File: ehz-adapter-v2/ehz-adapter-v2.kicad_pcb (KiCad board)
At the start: 2 copper layers, 32 x 32 mm, 16 parts, among them J1 Conn_02x10_Counter_Clockwise, J2 Conn_02x10_Counter_Clockwise, J3 Conn_01x02_Male, Q1 SFH 309 FA-5/6, Q2 BSS138, U1 LMV7235M7X, U2 D-SUN-MP1584EN

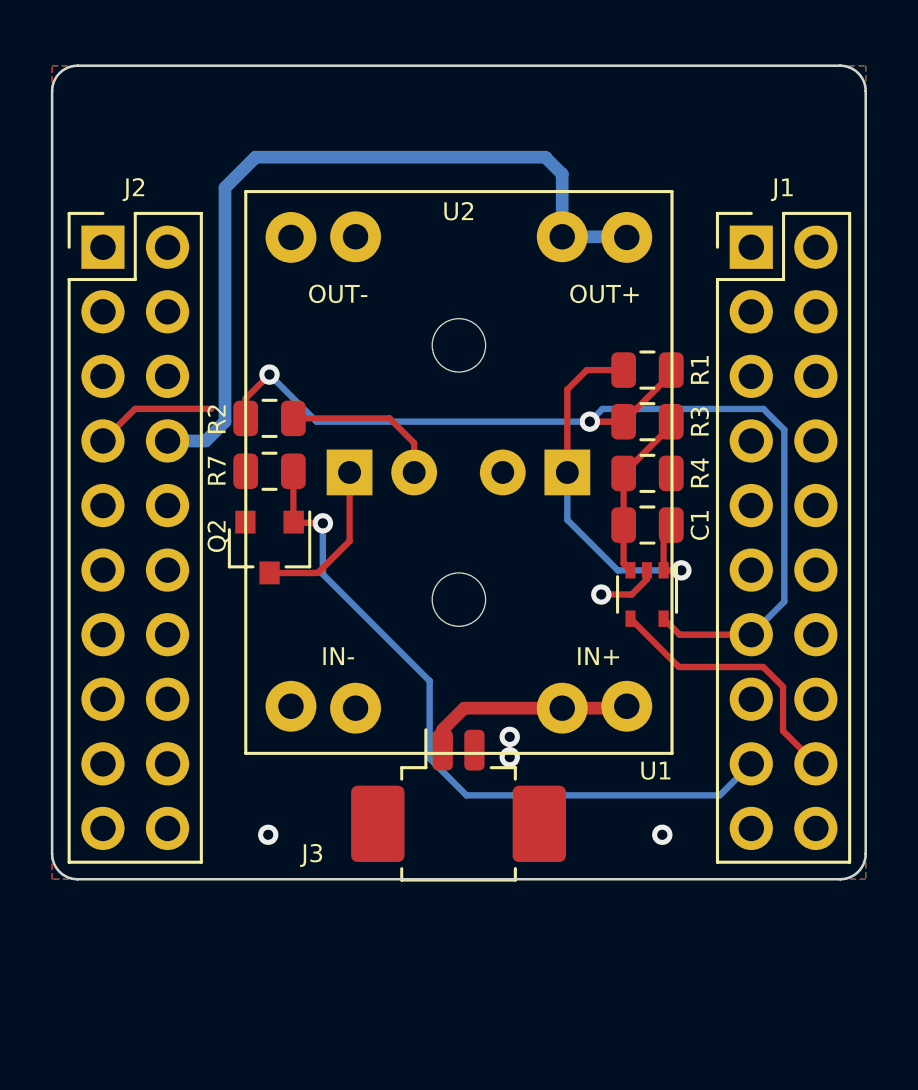
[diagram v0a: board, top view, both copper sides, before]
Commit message: moved mounting hooles
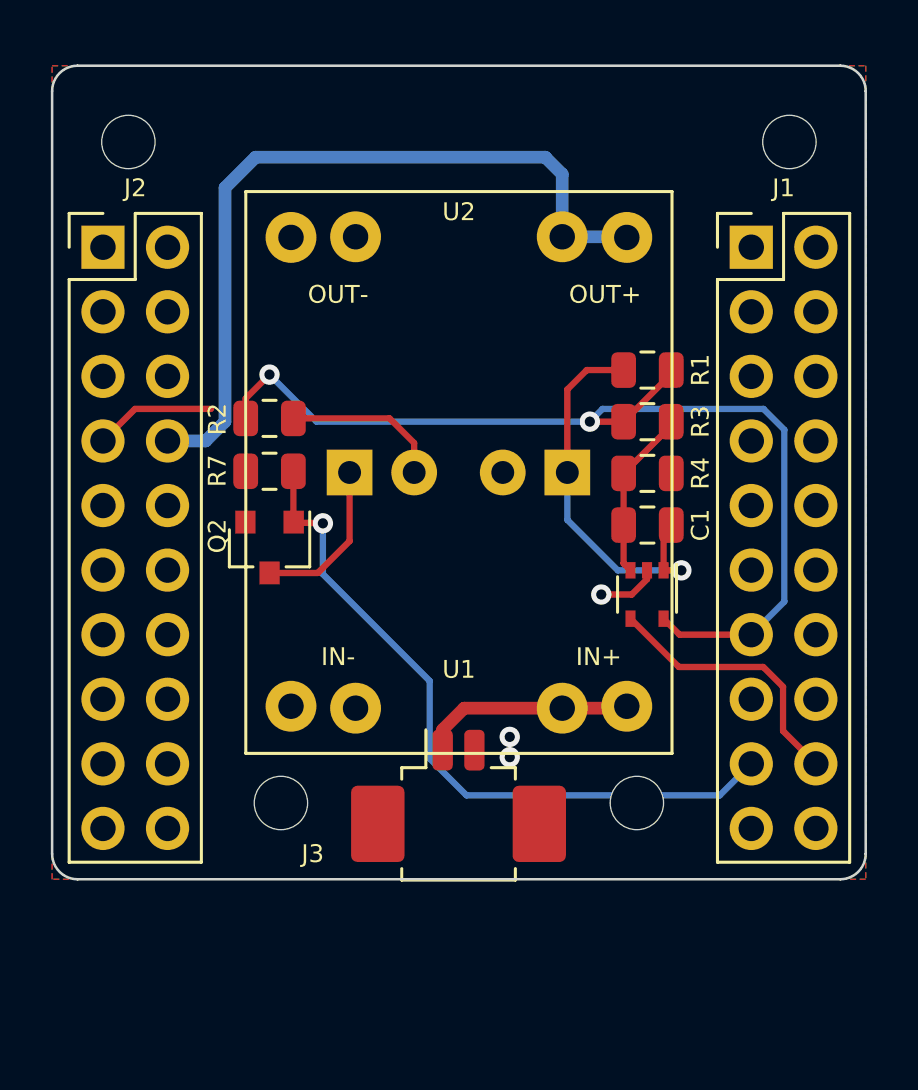
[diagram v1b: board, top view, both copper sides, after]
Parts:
- added H2: MountingHole, MountingHole:MountingHole_2.1mm, F.Cu at (48.0, 68.0)
- added H4: MountingHole, MountingHole:MountingHole_2.1mm, F.Cu at (60.7, 68.3)
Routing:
- net GND: vias 5 -> 3
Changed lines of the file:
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@@
     (grid_origin 40 40)
     (pcbplotparams
-      (layerselection 0x010fc_ffffffff)
+      (layerselection 0x010f0_ffffffff)
       (usegerberextensions false)
       (usegerberattributes true)
-      (usegerberadvancedattributes true)
-      (creategerberjobfile true)
+      (usegerberadvancedattributes false)
+      (creategerberjobfile false)
       (svguseinch false)
       (svgprecision 6)
-      (excludeedgelayer true)
+      (excludeedgelayer false)
       (linewidth 0.100000)
       (plotframeref false)
       (viasonmask false)
       (mode 1)
-      (useauxorigin false)
+      (useauxorigin true)
       (hpglpennumber 1)
       (hpglpenspeed 20)
@@
       (outputformat 1)
       (mirror false)
-      (drillshape 1)
+      (drillshape 0)
       (scaleselection 1)
-      (outputdirectory "")
+      (outputdirectory "gerber/")
     )
   )
@@
     (fp_circle (center 0 0) (end 2.1 0) (layer "Cmts.User") (width 0.15))
     (fp_circle (center 0 0) (end 2.35 0) (layer "F.CrtYd") (width 0.05))
-    (pad "" np_thru_hole circle (at 0 0 90) (size 2.1 2.1) (drill 2.1) (layers *.Cu *.Mask))
+    (pad "" np_thru_hole circle (at 8 -13 90) (size 2.1 2.1) (drill 2.1) (layers F&B.Cu *.Mask))
   )
   (module "Bouni:D-SUN-MP1584EN" (layer "F.Cu")
@@
       (rotate (xyz 0 0 0))
     )
+  )
+  (module "MountingHole:MountingHole_2.1mm" (layer "F.Cu")
+    (at 48 68)
+    (descr "Mounting Hole 2.1mm, no annular")
+    (tags "mounting hole 2.1mm no annular")
+    (property "Sheet file" "/home/bouni/projects/ehz-adapter-v2/ehz-adapter-v2/ehz-adapter-v2.kicad_sch")
+    (property "Sheet name" "")
+    (attr exclude_from_pos_files)
+    (fp_text reference "H2" (at 0 -3.2) (layer "F.SilkS") hide
+      (effects (font (size 1 1) (thickness 0.15)))
+    )
+    (fp_text value "MountingHole" (at 0 3.2) (layer "F.Fab")
+      (effects (font (size 1 1) (thickness 0.15)))
+    )
+    (fp_text user "${REFERENCE}" (at 0.3 0) (layer "F.Fab")
+      (effects (font (size 1 1) (thickness 0.15)))
+    )
+    (fp_circle (center 0 0) (end 2.1 0) (layer "Cmts.User") (width 0.15))
+    (fp_circle (center 0 0) (end 2.35 0) (layer "F.CrtYd") (width 0.05))
+    (pad "" np_thru_hole circle (at 0 0) (size 2.1 2.1) (drill 2.1) (layers F&B.Cu *.Mask))
   )
   (module "Connector_Molex:Molex_PicoBlade_53261-0271_1x02-1MP_P1.25mm_Horizontal" (layer "F.Cu")
@@
     (pad "2" smd roundrect (at 0.625 -2.4) (size 0.8 1.6) (layers "F.Cu" "F.Paste" "F.Mask") (roundrect_rratio 0.25)
       (net 3 "GND") (pinfunction "Pin_2"))
-    (pad "MP" smd roundrect (at 3.175 0.5) (size 2.1 3) (layers "F.Cu" "F.Paste" "F.Mask") (roundrect_rratio 0.119048))
-    (pad "MP" smd roundrect (at -3.175 0.5) (size 2.1 3) (layers "F.Cu" "F.Paste" "F.Mask") (roundrect_rratio 0.119048))
+    (pad "MP" smd roundrect (at 3.175 0.5) (size 2.1 3) (layers "F.Cu" "F.Paste" "F.Mask") (roundrect_rratio 0.1190480952380952))
+    (pad "MP" smd roundrect (at -3.175 0.5) (size 2.1 3) (layers "F.Cu" "F.Paste" "F.Mask") (roundrect_rratio 0.1190480952380952))
     (model "${KISYS3DMOD}/Connector_Molex.3dshapes/Molex_PicoBlade_53261-0271_1x02-1MP_P1.25mm_Horizontal.wrl"
       (offset (xyz 0 0 0))
@@
     (fp_circle (center 0 0) (end 2.1 0) (layer "Cmts.User") (width 0.15))
     (fp_circle (center 0 0) (end 2.35 0) (layer "F.CrtYd") (width 0.05))
-    (pad "" np_thru_hole circle (at 0 0 90) (size 2.1 2.1) (drill 2.1) (layers *.Cu *.Mask))
+    (pad "" np_thru_hole circle (at 18 13 90) (size 2.1 2.1) (drill 2.1) (layers F&B.Cu *.Mask))
   )
   (module "Package_TO_SOT_SMD:SOT-353_SC-70-5" (layer "F.Cu")
@@
     (property "Sheet name" "")
     (attr smd)
-    (fp_text reference "U1" (at 6.95 -0.35 180) (layer "F.SilkS")
+    (fp_text reference "U1" (at 2.95 7.4 180) (layer "F.SilkS")
       (effects (font (size 0.7 0.7) (thickness 0.1)))
     )
@@
     )
   )
+  (module "MountingHole:MountingHole_2.1mm" (layer "F.Cu")
+    (at 60.736 68.321)
+    (descr "Mounting Hole 2.1mm, no annular")
+    (tags "mounting hole 2.1mm no annular")
+    (property "Sheet file" "/home/bouni/projects/ehz-adapter-v2/ehz-adapter-v2/ehz-adapter-v2.kicad_sch")
+    (property "Sheet name" "")
+    (attr exclude_from_pos_files)
+    (fp_text reference "H4" (at 0 -3.2) (layer "F.SilkS") hide
+      (effects (font (size 1 1) (thickness 0.15)))
+    )
+    (fp_text value "MountingHole" (at 0 3.2) (layer "F.Fab")
+      (effects (font (size 1 1) (thickness 0.15)))
+    )
+    (fp_text user "${REFERENCE}" (at 0.3 0) (layer "F.Fab")
+      (effects (font (size 1 1) (thickness 0.15)))
+    )
+    (fp_circle (center 0 0) (end 2.1 0) (layer "Cmts.User") (width 0.15))
+    (fp_circle (center 0 0) (end 2.35 0) (layer "F.CrtYd") (width 0.05))
+    (pad "" np_thru_hole circle (at 1.264 -0.321) (size 2.1 2.1) (drill 2.1) (layers F&B.Cu *.Mask))
+  )
   (module "Connector_PinHeader_2.54mm:PinHeader_2x10_P2.54mm_Vertical" (layer "F.Cu")
     (at 66.5 46.14)
@@
   (segment (start 42.26 52.5) (end 45.25 52.5) (width 0.25) (layer "F.Cu") (net 3))
   (segment (start 61.8 59.8) (end 60.6 59.8) (width 0.25) (layer "F.Cu") (net 3))
-  (via (at 47.5 69.25) (size 0.8) (drill 0.4) (layers "F.Cu" "B.Cu") (net 3))
   (via (at 60.6 59.8) (size 0.8) (drill 0.4) (layers "F.Cu" "B.Cu") (net 3))
   (via (at 57 66.2) (size 0.8) (drill 0.4) (layers "F.Cu" "B.Cu") (net 3))
-  (via (at 63 69.25) (size 0.8) (drill 0.4) (layers "F.Cu" "B.Cu") (net 3))
   (via (at 57 65.4) (size 0.8) (drill 0.4) (layers "F.Cu" "B.Cu") (net 3))
   (segment (start 63.05 58.85) (end 63.75 58.85) (width 0.25) (layer "F.Cu") (net 4))

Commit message: fixed major layout fuckup, added MH-ET-LIVE-minikit footprint and symbol
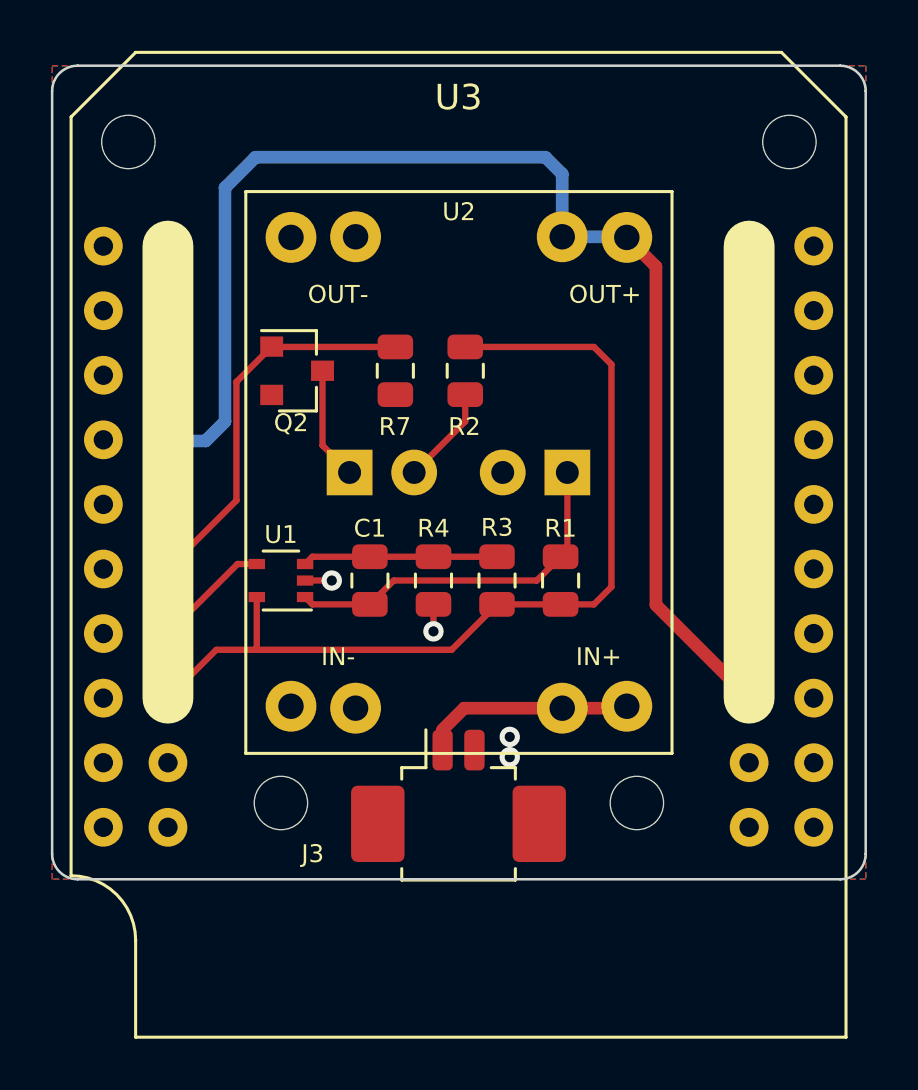
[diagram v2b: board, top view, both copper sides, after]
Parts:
- removed J1, J2: Conn_02x10_Counter_Clockwise, Connector_PinHeader_2.54mm:PinHeader_2x10_P2.54mm_Vertical
- added U3: mh-et-live-minikit, bouni:MH-ET LIVE MiniKit, F.Cu at (55.0, 57.5)
- moved H1 22.2 mm to (68.0, 42.0), turned to 0 degrees
- moved H3 15.3 mm to (42.0, 42.0), turned to 0 degrees
- moved U1 14.4 mm to (48.0, 59.2), turned to 180 degrees
- moved C1 11.1 mm to (51.5, 59.2), turned to 90 degrees
- moved R4 9.41 mm to (54.0, 59.2), turned to -90 degrees
- moved R1 8.96 mm to (59.0, 59.2), turned to 90 degrees
- moved R3 8.60 mm to (56.5, 59.2), turned to 90 degrees
- moved R2 7.92 mm to (55.2, 51.0), turned to -90 degrees
- moved Q2 7.04 mm to (48.6, 51.0), turned to 0 degrees
- moved R7 6.33 mm to (52.5, 51.0), turned to -90 degrees
- moved H4 1.30 mm to (62.0, 68.0)
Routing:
- net +5V: track 30.8 -> 50.9 mm
- net BLINK: track 27.9 -> 15.3 mm, vias 1 -> 0
- net RX: track 10.7 -> 4.63 mm
- net GND: track 7.17 -> 2.11 mm, vias 3 -> 4
- net +3V3: track 40.0 -> 36.1 mm, vias 2 -> 0
- net Net-(D1-Pad2): track 6.31 -> 3.90 mm
- net Net-(D1-Pad1): track 6.41 -> 4.44 mm
- net Net-(C1-Pad1): track 15.6 -> 14.4 mm, vias 1 -> 0
- net Net-(C1-Pad2): track 6.74 -> 7.67 mm
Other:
- board text added: "+"
- board text added: "-"
- board text added: "BLACK"
- board text added: "WHITE"

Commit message: fixed wrong comperator footprint, added alternative power pads
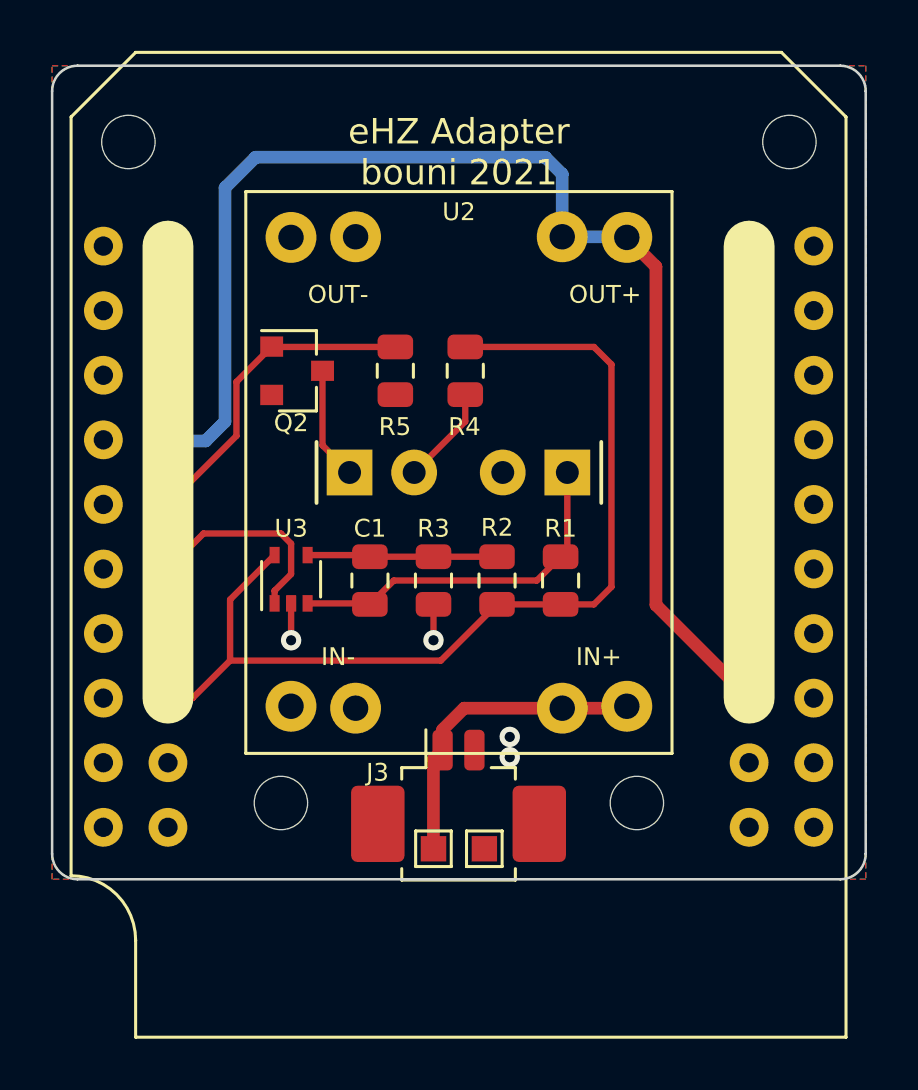
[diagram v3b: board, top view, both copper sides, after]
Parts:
- added TP1: TestPoint, TestPoint:TestPoint_Pad_1.0x1.0mm, F.Cu at (54.0, 69.8)
- added TP2: TestPoint, TestPoint:TestPoint_Pad_1.0x1.0mm, F.Cu at (56.0, 69.8)
- moved U3 0.40 mm to (48.4, 59.2), turned to 90 degrees
- renumbered R3 to R2, R4 to R3, R2 to R4, R7 to R5, U3 to U1, U1 to U3
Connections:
- U1 pad 15: (no net) -> BLINK
- U1 pad 16: BLINK -> RX
- U1 pad 17: RX -> (no net)
- U3 pad 1: Net-(C1-Pad1) -> RX
- U3 pad 3: Net-(C1-Pad2) -> Net-(C1-Pad1)
- U3 pad 4: RX -> Net-(C1-Pad2)
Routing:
- net Net-(J3-Pad1): track 8.43 -> 12.5 mm
- net RX: track 4.63 -> 8.21 mm
- net +3V3: track 36.1 -> 38.9 mm
- net BLINK: track 15.3 -> 12.8 mm
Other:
- board text added: "eHZ Adapter bouni 2021"

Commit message: replaced custom power connector pads
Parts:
- TP1, TP2: footprint TestPoint:TestPoint_Pad_1.0x1.0mm -> bouni:SolderPad1x3
- moved TP1 0.80 mm to (54.0, 69.0)
- moved TP2 0.80 mm to (56.0, 69.0)
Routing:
- net GND: vias 4 -> 2
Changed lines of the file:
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@@
     (pad "" np_thru_hole circle (at 0 0) (size 2.1 2.1) (drill 2.1) (layers *.Cu *.Mask))
   )
-  (module "TestPoint:TestPoint_Pad_1.0x1.0mm" (layer "F.Cu")
-    (at 56 69.8)
-    (descr "SMD rectangular pad as test Point, square 1.0mm side length")
-    (tags "test point SMD pad rectangle square")
-    (property "Dateiname Blatt" "C:/Projekte/KiCAD/ehz-apdapter-v2/ehz-adapter-v2/ehz-adapter-v2.kicad_sch")
-    (property "Schaltplanname" "")
-    (attr exclude_from_pos_files)
-    (fp_text reference "TP2" (at 0 -1.448) (layer "F.SilkS") hide
-      (effects (font (size 1 1) (thickness 0.15)))
-    )
-    (fp_text value "TestPoint" (at 0 1.55) (layer "F.Fab") hide
-      (effects (font (size 1 1) (thickness 0.15)))
-    )
-    (fp_text user "${REFERENCE}" (at 0 -1.45) (layer "F.Fab") hide
-      (effects (font (size 1 1) (thickness 0.15)))
-    )
-    (fp_line (start -0.7 -0.7) (end 0.7 -0.7) (layer "F.SilkS") (width 0.12))
-    (fp_line (start 0.7 -0.7) (end 0.7 0.7) (layer "F.SilkS") (width 0.12))
-    (fp_line (start -0.7 0.7) (end -0.7 -0.7) (layer "F.SilkS") (width 0.12))
-    (fp_line (start 0.7 0.7) (end -0.7 0.7) (layer "F.SilkS") (width 0.12))
-    (fp_line (start -1 -1) (end 1 -1) (layer "F.CrtYd") (width 0.05))
-    (fp_line (start 1 1) (end -1 1) (layer "F.CrtYd") (width 0.05))
-    (fp_line (start 1 1) (end 1 -1) (layer "F.CrtYd") (width 0.05))
-    (fp_line (start -1 -1) (end -1 1) (layer "F.CrtYd") (width 0.05))
-    (pad "1" smd rect (at 0 0) (size 1 1) (layers "F.Cu" "F.Mask")
+  (module "bouni:SolderPad1x3" (layer "F.Cu")
+    (at 56 69)
+    (property "Dateiname Blatt" "C:/Projekte/KiCAD/ehz-apdapter-v2/ehz-adapter-v2/ehz-adapter-v2.kicad_sch")
+    (property "Schaltplanname" "")
+    (attr through_hole)
+    (fp_text reference "TP2" (at 0 -3.8 unlocked) (layer "F.SilkS") hide
+      (effects (font (size 1 1) (thickness 0.15)))
+    )
+    (fp_text value "TestPoint" (at 0 -2.3 unlocked) (layer "F.Fab") hide
+      (effects (font (size 1 1) (thickness 0.15)))
+    )
+    (pad "1" smd rect (at 0 0) (size 1 3) (layers "F.Cu" "F.Paste" "F.Mask")
       (net 3 "GND") (pinfunction "1"))
   )
@@
     (property "Schaltplanname" "")
     (attr smd)
-    (fp_text reference "J3" (at -3.186 -1.521) (layer "F.SilkS")
+    (fp_text reference "J3" (at -4.986 1.679) (layer "F.SilkS")
       (effects (font (size 0.7 0.7) (thickness 0.1)))
     )
@@
     (pad "" np_thru_hole circle (at 0 0) (size 2.1 2.1) (drill 2.1) (layers *.Cu *.Mask))
   )
-  (module "TestPoint:TestPoint_Pad_1.0x1.0mm" (layer "F.Cu")
-    (at 54 69.8)
-    (descr "SMD rectangular pad as test Point, square 1.0mm side length")
-    (tags "test point SMD pad rectangle square")
-    (property "Dateiname Blatt" "C:/Projekte/KiCAD/ehz-apdapter-v2/ehz-adapter-v2/ehz-adapter-v2.kicad_sch")
-    (property "Schaltplanname" "")
-    (attr exclude_from_pos_files)
-    (fp_text reference "TP1" (at 0 -1.448) (layer "F.SilkS") hide
-      (effects (font (size 1 1) (thickness 0.15)))
-    )
-    (fp_text value "TestPoint" (at 0 1.55) (layer "F.Fab") hide
-      (effects (font (size 1 1) (thickness 0.15)))
-    )
-    (fp_text user "${REFERENCE}" (at 0 -1.45) (layer "F.Fab") hide
-      (effects (font (size 1 1) (thickness 0.15)))
-    )
-    (fp_line (start -0.7 -0.7) (end 0.7 -0.7) (layer "F.SilkS") (width 0.12))
-    (fp_line (start 0.7 0.7) (end -0.7 0.7) (layer "F.SilkS") (width 0.12))
-    (fp_line (start 0.7 -0.7) (end 0.7 0.7) (layer "F.SilkS") (width 0.12))
-    (fp_line (start -0.7 0.7) (end -0.7 -0.7) (layer "F.SilkS") (width 0.12))
-    (fp_line (start -1 -1) (end -1 1) (layer "F.CrtYd") (width 0.05))
-    (fp_line (start 1 1) (end -1 1) (layer "F.CrtYd") (width 0.05))
-    (fp_line (start -1 -1) (end 1 -1) (layer "F.CrtYd") (width 0.05))
-    (fp_line (start 1 1) (end 1 -1) (layer "F.CrtYd") (width 0.05))
-    (pad "1" smd rect (at 0 0) (size 1 1) (layers "F.Cu" "F.Mask")
+  (module "bouni:SolderPad1x3" (layer "F.Cu")
+    (at 54 69)
+    (property "Dateiname Blatt" "C:/Projekte/KiCAD/ehz-apdapter-v2/ehz-adapter-v2/ehz-adapter-v2.kicad_sch")
+    (property "Schaltplanname" "")
+    (attr through_hole)
+    (fp_text reference "TP1" (at 0 -3.8 unlocked) (layer "F.SilkS") hide
+      (effects (font (size 1 1) (thickness 0.15)))
+    )
+    (fp_text value "TestPoint" (at 0 -2.3 unlocked) (layer "F.Fab") hide
+      (effects (font (size 1 1) (thickness 0.15)))
+    )
+    (pad "1" smd rect (at 0 0) (size 1 3) (layers "F.Cu" "F.Paste" "F.Mask")
       (net 10 "Net-(J3-Pad1)") (pinfunction "1"))
   )
@@
     (effects (font (size 1 1) (thickness 0.15)) (justify mirror))
   )
+  (gr_text "-" (at 57 65.8) (layer "F.SilkS")
+    (effects (font (size 1.5 1.5) (thickness 0.3)))
+  )
   (gr_text "eHZ Adapter\nbouni 2021" (at 55 42.4) (layer "F.SilkS")
     (effects (font (size 1 1) (thickness 0.15)))
+  )
+  (gr_text "+" (at 52.8 65.8) (layer "F.SilkS")
+    (effects (font (size 1.5 1.5) (thickness 0.3)))
   )
   (segment (start 55.25 52.99) (end 55.25 51.9375) (width 0.25) (layer "F.Cu") (net 1))
@@
   (via (at 54 61.6) (size 0.8) (drill 0.4) (layers "F.Cu" "B.Cu") (net 3))
   (via (at 48.4 61.6) (size 0.8) (drill 0.4) (layers "F.Cu" "B.Cu") (net 3))
-  (via (at 57 66.2) (size 0.8) (drill 0.4) (layers "F.Cu" "B.Cu") (net 3))
-  (via (at 57 65.4) (size 0.8) (drill 0.4) (layers "F.Cu" "B.Cu") (net 3))
   (segment (start 58.0625 59.25) (end 59 58.3125) (width 0.25) (layer "F.Cu") (net 4))
   (segment (start 51.5 60.1875) (end 52.4375 59.25) (width 0.25) (layer "F.Cu") (net 4))

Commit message: last minor fixes before ordering at JLCPCB
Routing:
- net GND: track 2.11 -> 5.35 mm
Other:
- board text added: "JLCJLCJLCJLC"
